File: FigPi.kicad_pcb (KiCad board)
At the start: 2 copper layers, 25.8 x 40.4 mm, 35 parts, among them J1 MOLEX_47346-100147346, J2 Debug, J3 PMW3/PMW4, J4 I2C1/PMW1, J5 SPI0/PWM2/PWM3, J6 I2C0/PMW0, J7 ADC/UART0/UART0/UART1/PWM5/PW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, SW1 KMS233GLFG, SW2 KMS233GLFG, U1 RP2040, U2 QSPI NOR FLASH 2MiB 2x3mm USO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, U3 AP2112K-3.3, U4 KC2520Z

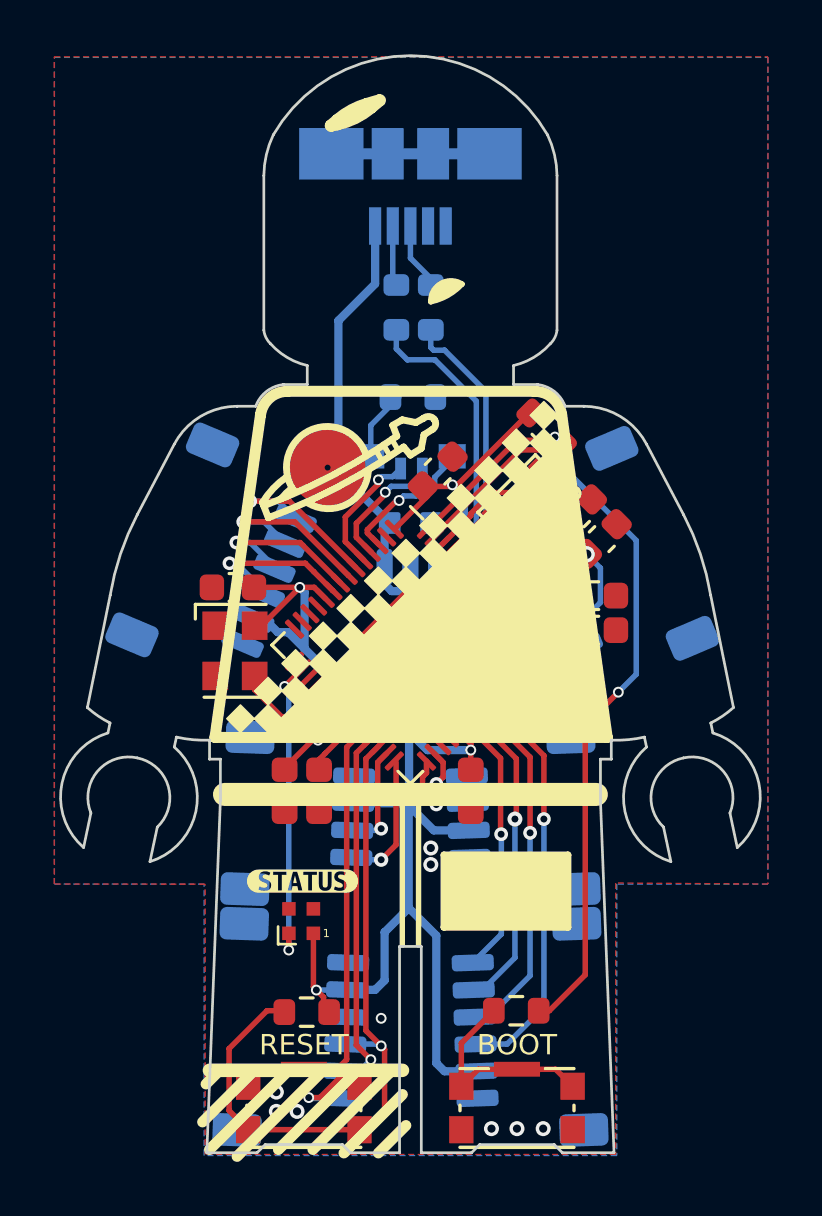
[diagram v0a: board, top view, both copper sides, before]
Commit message: Connected USBOOT properly to Boot button.  Had to move capacitor for new track.
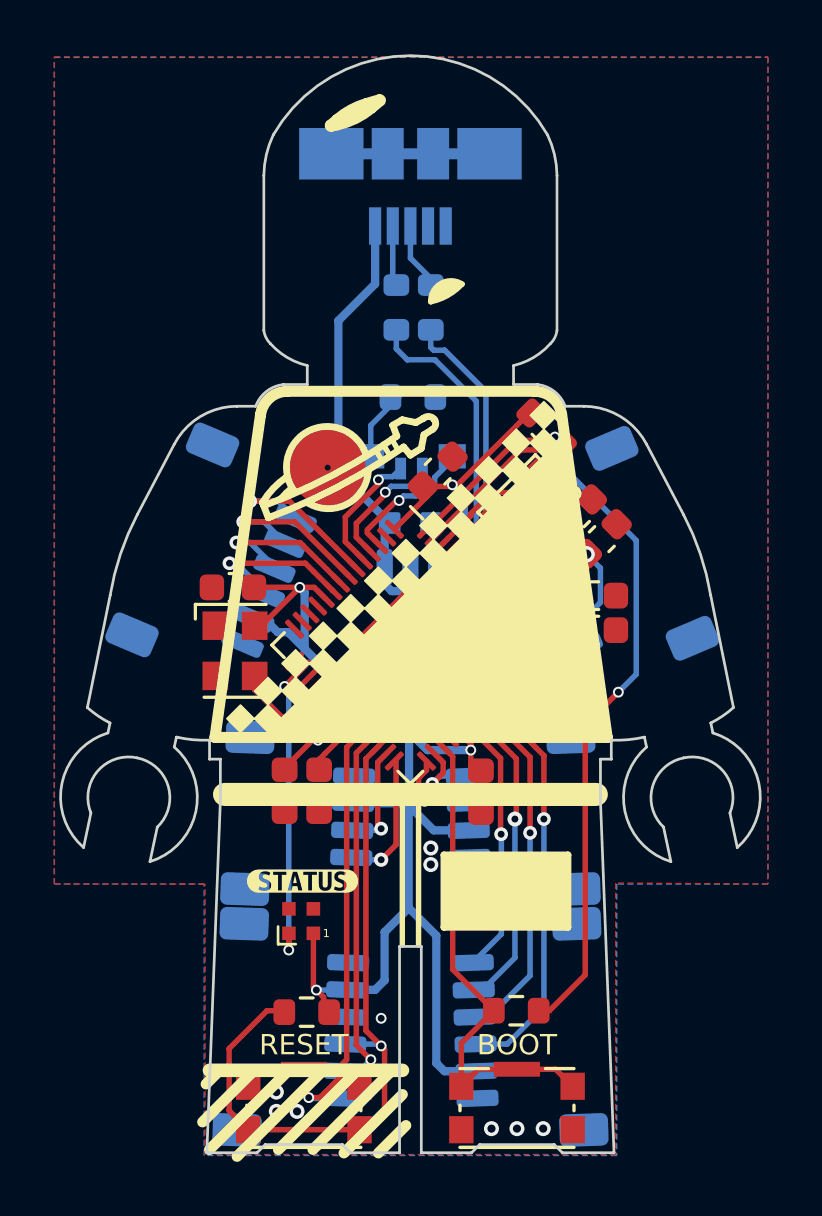
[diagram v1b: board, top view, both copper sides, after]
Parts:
- R7: value R -> 27R
- moved C12 0.38 mm to (14.6, -13.3)
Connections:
- U1 pad 31: unconnected-(U1-Pad31) -> /~{USB_BOOT}
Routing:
- net /~{USB_BOOT}: track 8.02 -> 18.6 mm
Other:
- board text added: "Fig Pi v1.1"
- board text removed: "Fig Pi v1.0"

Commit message: v1.5 - Changed all JST connections to 4-pin.  Added 8 additional APA102 - 2020 LEDs for a 3 x 3 matrix.  Rearranged items as needed.  Moved SWDIO and SWCLK from JST connector to test pads.
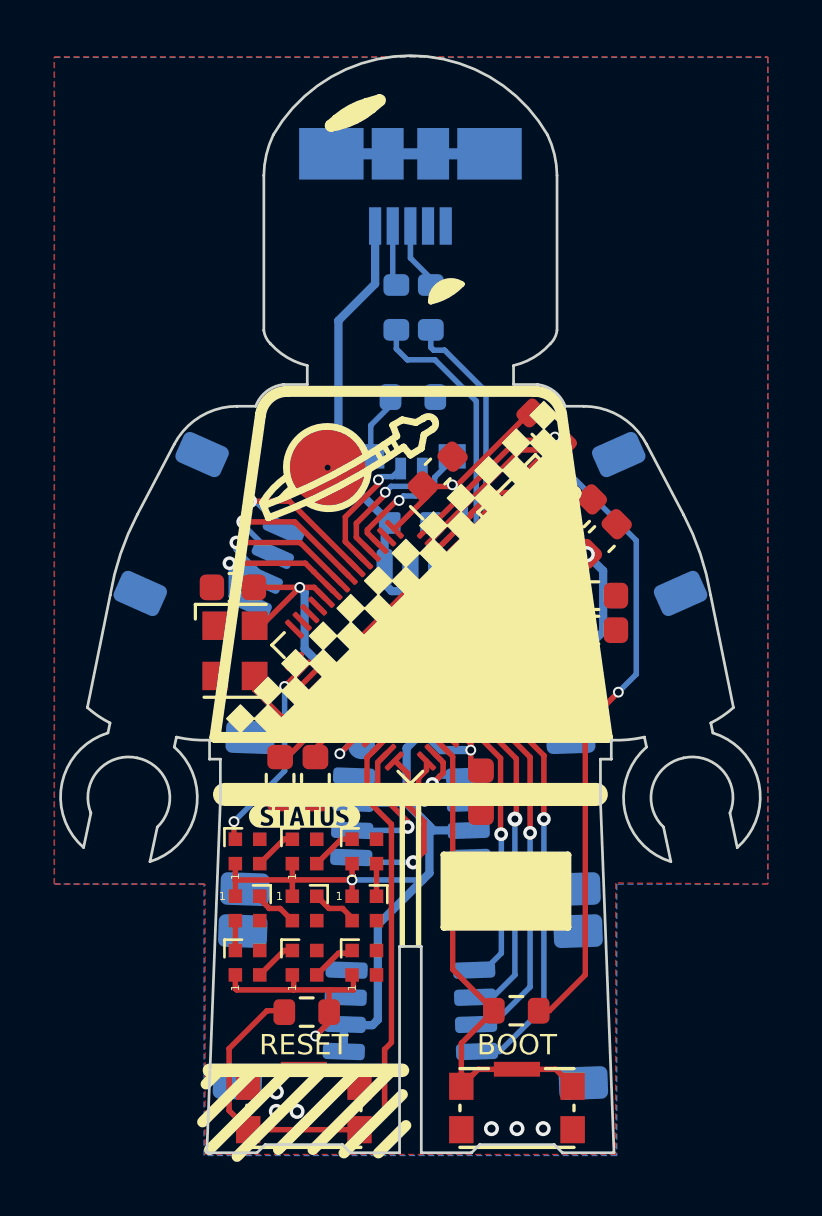
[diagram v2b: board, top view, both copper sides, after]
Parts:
- added D12: WS2812B, LED_SMD:LED_SK6812_EC15_1.5x1.5mm, F.Cu at (10.3, -11.1)
- added D13: WS2812B, LED_SMD:LED_SK6812_EC15_1.5x1.5mm, F.Cu at (6.00, -9.00)
- added D2: WS2812B, LED_SMD:LED_SK6812_EC15_1.5x1.5mm, F.Cu at (10.3, -9.00)
- added D3: WS2812B, LED_SMD:LED_SK6812_EC15_1.5x1.5mm, F.Cu at (6.00, -7.00)
- added D5: WS2812B, LED_SMD:LED_SK6812_EC15_1.5x1.5mm, F.Cu at (8.10, -7.00)
- added D6: WS2812B, LED_SMD:LED_SK6812_EC15_1.5x1.5mm, F.Cu at (10.3, -7.00)
- added D7: WS2812B, LED_SMD:LED_SK6812_EC15_1.5x1.5mm, F.Cu at (8.10, -11.1)
- added D8: WS2812B, LED_SMD:LED_SK6812_EC15_1.5x1.5mm, F.Cu at (8.10, -9.00)
- added TP1: TestPoint, TestPoint:TestPoint_Pad_D1.0mm, B.Cu at (10.2, -15.0)
- added TP2: TestPoint, TestPoint:TestPoint_Pad_D1.0mm, B.Cu at (10.2, -16.6)
- J2: value Debug -> SPI0 / PWM2 / PWM3; footprint Connector_JST:JST_SH_SM06B-SRSS-TB_1x06-1MP_P1.00mm_Horizontal -> Connector_JST:JST_SH_SM04B-SRSS-TB_1x04-1MP_P1.00mm_Horizontal
- J3: value PMW3/PMW4 -> UART0 / PWM3 / PWM4; footprint Connector_JST:JST_SH_SM06B-SRSS-TB_1x06-1MP_P1.00mm_Horizontal -> Connector_JST:JST_SH_SM04B-SRSS-TB_1x04-1MP_P1.00mm_Horizontal
- J4: value I2C1/PMW1 -> STEMMA_1/QWIIC_1/I2C1/PMW1
- J5: value SPI0/PWM2/PWM3 -> ADC / PWM5 / PWM6; footprint Connector_JST:JST_SH_SM06B-SRSS-TB_1x06-1MP_P1.00mm_Horizontal -> Connector_JST:JST_SH_SM04B-SRSS-TB_1x04-1MP_P1.00mm_Horizontal
- J6: value I2C0/PMW0 -> STEMMA_0/QWIIC_0/I2C0/PMW0
- J7: value ADC/UART0/UART0/UART1/PWM5/PWM6 -> PWR; footprint Connector_JST:JST_SH_SM06B-SRSS-TB_1x06-1MP_P1.00mm_Horizontal -> Connector_JST:JST_SH_SM04B-SRSS-TB_1x04-1MP_P1.00mm_Horizontal
- moved J7 20.1 mm to (7.60, -5.30), turned to 88 degrees
- moved J2 18.0 mm to (4.90, -22.4), turned to 66 degrees
- moved J5 14.2 mm to (19.1, -22.4), turned to -66 degrees
- moved D4 3.24 mm to (6.00, -11.1), turned to 90 degrees
- moved kibuzzard-620D4CA4 2.39 mm to (8.10, -12.4)
- moved J3 0.73 mm to (16.4, -5.30)
- moved C8 0.49 mm to (7.20, -13.8)
- moved C3 0.48 mm to (8.50, -13.8)
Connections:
- net Net-(J3-Pad3) renamed /TX
- net Net-(J3-Pad4) renamed /RX
- net Net-(J4-Pad1) renamed /SCL1
- net Net-(J4-Pad2) renamed /SDA1
- net Net-(J6-Pad1) renamed /SCL/D5
- net Net-(J6-Pad2) renamed /SDA/D4
- D4 pad 2: unconnected-(D4-Pad2) -> Net-(D4-Pad2)
- J2 pad 1: /SWCLK -> /MOSI/D10
- J2 pad 2: /SWDIO -> /SCK/D8
- J2 pad 3: /RUN -> /D14
- J2 pad 4: unconnected-(J2-Pad4) -> /MISO/D9
- J5 pad 1: GND -> /A3/D3
- J5 pad 2: +3V3 -> /A2/D2
- J5 pad 3: Net-(J5-Pad3) -> /A1/D1
- J5 pad 4: Net-(J5-Pad4) -> /A0/D0
- J7 pad 1: Net-(J7-Pad1) -> +3V3
- J7 pad 2: Net-(J7-Pad2) -> +3V3
- J7 pad 3: Net-(J7-Pad3) -> GND
- J7 pad 4: Net-(J7-Pad4) -> GND
- U1 pad 38: Net-(J7-Pad1) -> /A3/D3
- U1 pad 39: Net-(J7-Pad2) -> /A2/D2
- U1 pad 40: Net-(J7-Pad3) -> /A1/D1
- U1 pad 41: Net-(J7-Pad4) -> /A0/D0
- U1 pad 6: Net-(J5-Pad6) -> /MISO/D9
- U1 pad 7: Net-(J5-Pad5) -> /D14
- U1 pad 8: Net-(J5-Pad4) -> /SCK/D8
- U1 pad 9: Net-(J5-Pad3) -> /MOSI/D10
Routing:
- net /SWCLK: track 15.9 -> 2.16 mm
- net /SWDIO: track 13.5 -> 2.39 mm
- net +3V3: track 98.9 -> 107.2 mm
- net /A2/D2: track 0.00 -> 7.26 mm, vias 0 -> 1
- net Net-(J7-Pad2): track 7.22 -> 0.00 mm, vias 1 -> 0
- net Net-(J7-Pad1): track 7.14 -> 0.00 mm, vias 1 -> 0
- net /A3/D3: track 0.00 -> 6.99 mm, vias 0 -> 1
- net Net-(J5-Pad6): track 6.85 -> 0.00 mm, vias 1 -> 0
- net /MISO/D9: track 0.00 -> 6.59 mm, vias 0 -> 1
- net Net-(J5-Pad5): track 6.57 -> 0.00 mm, vias 1 -> 0
- net /D14: track 0.00 -> 6.34 mm, vias 0 -> 1
- net /MOSI/D10: track 0.00 -> 6.31 mm, vias 0 -> 1
- net Net-(J5-Pad4): track 6.29 -> 0.00 mm, vias 1 -> 0
- net /SCK/D8: track 0.00 -> 6.19 mm, vias 0 -> 1
- net Net-(J5-Pad3): track 6.02 -> 0.00 mm, vias 1 -> 0
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- removed copper zone on F.Cu, net (none)
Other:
- board text added: "C"
- board text added: "D"
- board text added: "Fig Pi v1.5"
- board text removed: "Fig Pi v1.1"

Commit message: 1.6 - Minor Cosmetic Changes
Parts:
- moved C8 0.32 mm to (7.10, -14.1)
- moved C3 0.30 mm to (8.45, -14.1)
- moved kibuzzard-620D4CA4 0.05 mm to (8.15, -12.4)
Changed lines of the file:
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@@
   )
   (footprint "Capacitor_SMD:C_0603_1608Metric" (layer "F.Cu")
-    (at 7.2 -13.8 90)
+    (at 7.1 -14.1 90)
     (descr "Capacitor SMD 0603 (1608 Metric), square (rectangular) end terminal, IPC_7351 nominal, (Body size source: IPC-SM-782 page 76, https://www.pcb-3d.com/wordpress/wp-content/uploads/ipc-sm-782a_amendment_1_and_2.pdf), generated with kicad-footprint-generator")
     (tags "capacitor")
@@
   )
   (footprint "Capacitor_SMD:C_0603_1608Metric" (layer "F.Cu")
-    (at 8.5 -13.8 90)
+    (at 8.45 -14.1 90)
     (descr "Capacitor SMD 0603 (1608 Metric), square (rectangular) end terminal, IPC_7351 nominal, (Body size source: IPC-SM-782 page 76, https://www.pcb-3d.com/wordpress/wp-content/uploads/ipc-sm-782a_amendment_1_and_2.pdf), generated with kicad-footprint-generator")
     (tags "capacitor")
@@
   )
   (footprint "kibuzzard-620D4CA4" (layer "F.Cu")
-    (at 8.1 -12.4)
+    (at 8.15 -12.4)
     (descr "Converted using: scripting")
     (tags "svg2mod")
@@
   (gr_line (start 11.7 -13.35) (end 11.7 -7.65) (layer "F.SilkS") (width 0.2))
   (gr_arc (start 6.478558 -27.189797) (mid 6.812918 -27.804917) (end 7.46874 -28.05) (layer "F.SilkS") (width 0.4064))
-  (gr_line (start 18.85 -13.2) (end 5.15 -13.2) (layer "F.SilkS") (width 0.85))
+  (gr_line (start 18.85 -13.8) (end 5.15 -13.8) (layer "F.SilkS") (width 0.85))
   (gr_line (start 16.581259 -28.05) (end 7.46874 -28.05) (layer "F.SilkS") (width 0.4064))
   (gr_arc (start 16.581257 -28.05) (mid 17.23708 -27.804917) (end 17.57144 -27.189796) (layer "F.SilkS") (width 0.4064))
@@
   (segment (start 5.55 -6.05) (end 5.55 -6.55) (width 0.2032) (layer "F.Cu") (net 3))
   (segment (start 18.021 -18.679) (end 18.021 -19.2532) (width 0.3048) (layer "F.Cu") (net 3))
+  (segment (start 7.1 -14.875) (end 7.925 -15.7) (width 0.2032) (layer "F.Cu") (net 3))
   (segment (start 9.0038 -5.9962) (end 9 -6) (width 0.2032) (layer "F.Cu") (net 3))
   (segment (start 18.3 -18.4) (end 18.177208 -18.277208) (width 0.3048) (layer "F.Cu") (net 3))
+  (segment (start 7.925 -15.7) (end 8.9 -15.7) (width 0.2032) (layer "F.Cu") (net 3))
   (segment (start 9.282843 -15.7) (end 9.710742 -16.127899) (width 0.2032) (layer "F.Cu") (net 3))
   (segment (start 18.021 -18.964616) (end 17.333592 -18.277208) (width 0.2032) (layer "F.Cu") (net 3))
-  (segment (start 8.9 -15.7) (end 8.591 -15.7) (width 0.2032) (layer "F.Cu") (net 3))
   (segment (start 18.021 -20.5232) (end 18.454002 -20.090198) (width 0.2032) (layer "F.Cu") (net 3))
   (segment (start 7.65 -10.15) (end 7.65 -10.75) (width 0.2032) (layer "F.Cu") (net 3))
@@
   (segment (start 9.9 -6.5) (end 9.9 -6) (width 0.2032) (layer "F.Cu") (net 3))
   (segment (start 17.500155 -20.5232) (end 18.021 -20.5232) (width 0.2032) (layer "F.Cu") (net 3))
-  (segment (start 8.591 -15.7) (end 7.493 -14.602) (width 0.2032) (layer "F.Cu") (net 3))
   (segment (start 17.075658 -22.005596) (end 18.249588 -22.005596) (width 0.2032) (layer "F.Cu") (net 3))
   (segment (start 15.986314 -19.575045) (end 16.269157 -19.292202) (width 0.2032) (layer "F.Cu") (net 3))
@@
   (segment (start 13.875 -2.45) (end 13.85 -2.45) (width 0.2032) (layer "F.Cu") (net 28))
   (segment (start 14.5 -3.075) (end 13.875 -2.45) (width 0.2032) (layer "F.Cu") (net 28))
-  (segment (start 13.559081 -6.748719) (end 15.0754 -5.2324) (width 0.2) (layer "F.Cu") (net 28))
+  (segment (start 13.1 -7.2078) (end 13.1 -11.6) (width 0.2) (layer "F.Cu") (net 28))
   (segment (start 15.925 -3.075) (end 17.35 -3.075) (width 0.2032) (layer "F.Cu") (net 28))
   (segment (start 17.35 -3.075) (end 17.975 -2.45) (width 0.2032) (layer "F.Cu") (net 28))
-  (segment (start 13.559081 -14.595334) (end 13.559081 -6.748719) (width 0.2) (layer "F.Cu") (net 28))
+  (segment (start 13.1 -11.6) (end 13.6 -12.1) (width 0.2) (layer "F.Cu") (net 28))
+  (segment (start 15.0754 -5.2324) (end 13.1 -7.2078) (width 0.2) (layer "F.Cu") (net 28))
   (segment (start 13.875 -4.032) (end 15.0754 -5.2324) (width 0.2032) (layer "F.Cu") (net 28))
-  (segment (start 13.157887 -14.996528) (end 13.559081 -14.595334) (width 0.2) (layer "F.Cu") (net 28))
+  (segment (start 13.6 -12.1) (end 13.6 -14.554415) (width 0.2) (layer "F.Cu") (net 28))
+  (segment (start 13.6 -14.554415) (end 13.157887 -14.996528) (width 0.2) (layer "F.Cu") (net 28))
   (segment (start 13.875 -2.45) (end 13.875 -4.032) (width 0.2032) (layer "F.Cu") (net 28))
   (segment (start 17.907 -2.518) (end 17.975 -2.45) (width 0.2032) (layer "F.Cu") (net 28))
@@
   (segment (start 10.935599 -24.905599) (end 11.341199 -24.905599) (width 0.2032) (layer "B.Cu") (net 35))
   (segment (start 11.341199 -24.905599) (end 11.6396 -25.204) (width 0.2032) (layer "B.Cu") (net 35))
+  (segment (start 7.2172 -16.1) (end 6.2622 -17.055) (width 0.2032) (layer "F.Cu") (net 36))
+  (segment (start 8.551471 -16.1) (end 7.2172 -16.1) (width 0.2032) (layer "F.Cu") (net 36))
   (segment (start 6.2622 -17.055) (end 6.2622 -17.5662) (width 0.2032) (layer "F.Cu") (net 36))
-  (segment (start 8.504271 -16.0528) (end 7.2644 -16.0528) (width 0.2032) (layer "F.Cu") (net 36))
-  (segment (start 9.145056 -16.693585) (end 8.504271 -16.0528) (width 0.2032) (layer "F.Cu") (net 36))
-  (segment (start 7.2644 -16.0528) (end 6.2622 -17.055) (width 0.2032) (layer "F.Cu") (net 36))
+  (segment (start 9.145056 -16.693585) (end 8.551471 -16.1) (width 0.2032) (layer "F.Cu") (net 36))
   (segment (start 15.321099 -14.530372) (end 15.321099 -11.755301) (width 0.2032) (layer "F.Cu") (net 39))
   (segment (start 15.321099 -11.755301) (end 15.3416 -11.7348) (width 0.2032) (layer "F.Cu") (net 39))

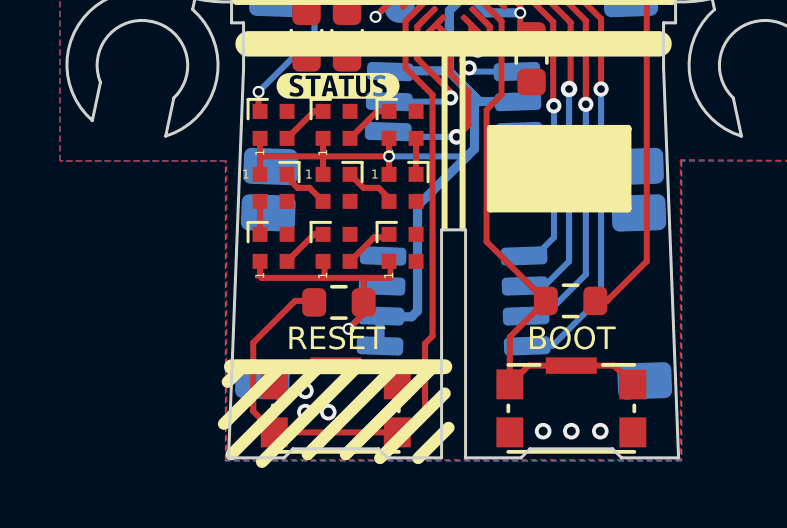
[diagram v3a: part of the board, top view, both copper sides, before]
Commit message: v1.7 Fixed potential manufacturing limitation with ground vias.
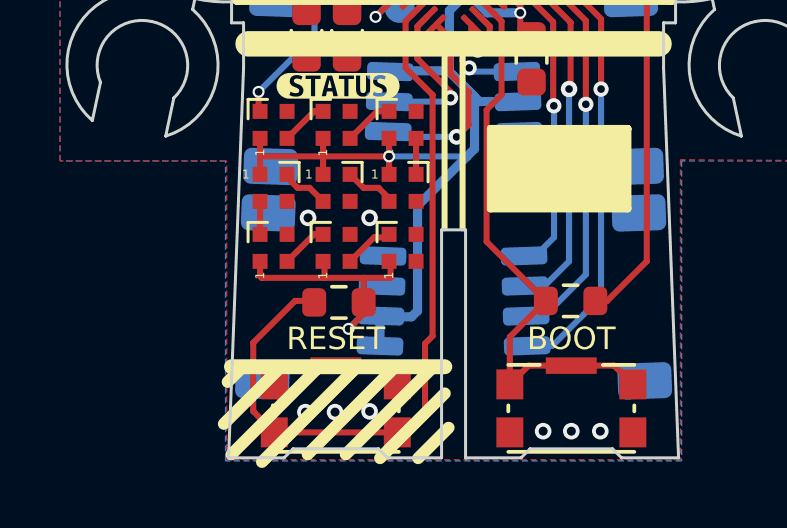
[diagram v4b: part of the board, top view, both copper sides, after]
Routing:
- net GND: vias 12 -> 14
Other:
- board text added: "Fig Pi v1.7"
- board text removed: "Fig Pi v1.5"
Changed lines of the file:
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@@
     (effects (font (size 1 1) (thickness 0.15)) (justify mirror))
   )
-  (gr_text "Fig Pi\nv1.5" (at 12.0396 -8.9408) (layer "B.SilkS")
+  (gr_text "Fig Pi\nv1.7" (at 12.0396 -8.9408) (layer "B.SilkS")
     (effects (font (size 0.8 0.8) (thickness 0.15)) (justify mirror))
   )
@@
   (via (at 10.237 -18.669) (size 0.604) (drill 0.35) (layers "F.Cu" "B.Cu") (net 1))
   (via (at 13.716 -18.664) (size 0.604) (drill 0.35) (layers "F.Cu" "B.Cu") (net 1))
-  (via (at 7.0612 -2.2352) (size 0.554) (drill 0.3) (layers "F.Cu" "B.Cu") (net 1))
+  (via (at 9.2 -1.55) (size 0.554) (drill 0.3) (layers "F.Cu" "B.Cu") (net 1))
   (via (at 12 -19.9) (size 0.604) (drill 0.35) (layers "F.Cu" "B.Cu") (net 1))
   (via (at 16.891 -0.889) (size 0.554) (drill 0.3) (layers "F.Cu" "B.Cu") (net 1))
@@
   (via (at 14.986 -0.889) (size 0.554) (drill 0.3) (layers "F.Cu" "B.Cu") (net 1))
   (via (at 15.925 -0.889) (size 0.554) (drill 0.3) (layers "F.Cu" "B.Cu") (net 1))
+  (via (at 7.15 -8) (size 0.554) (drill 0.3) (layers "F.Cu" "B.Cu") (net 1))
+  (via (at 9.2 -8) (size 0.554) (drill 0.3) (layers "F.Cu" "B.Cu") (net 1))
   (via (at 7.0612 -1.524) (size 0.554) (drill 0.3) (layers "F.Cu" "B.Cu") (net 1))
-  (via (at 7.8232 -1.524) (size 0.554) (drill 0.3) (layers "F.Cu" "B.Cu") (net 1))
+  (via (at 8.05 -1.524) (size 0.554) (drill 0.3) (layers "F.Cu" "B.Cu") (net 1))
   (via (at 12 -16.9) (size 0.604) (drill 0.35) (layers "F.Cu" "B.Cu") (net 1))
   (segment (start 11.1625 -36.8) (end 9.0875 -36.8) (width 0.4064) (layer "B.Cu") (net 1))
